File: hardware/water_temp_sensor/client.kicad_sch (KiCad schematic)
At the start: 7 parts, among them J1 AVR-ISP-6, U1 DS18B20, U2 DS18B20

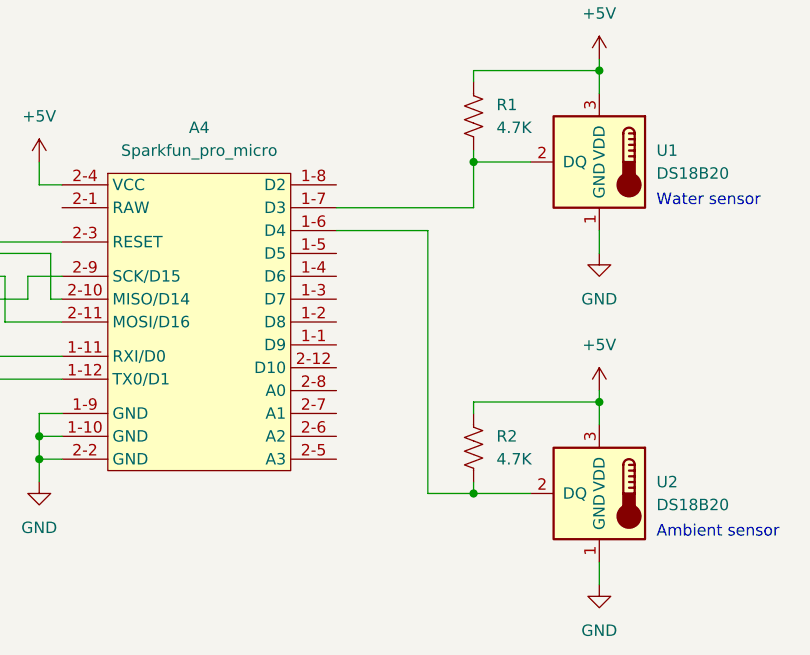
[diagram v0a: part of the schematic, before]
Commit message: Turn off status led for power reduction
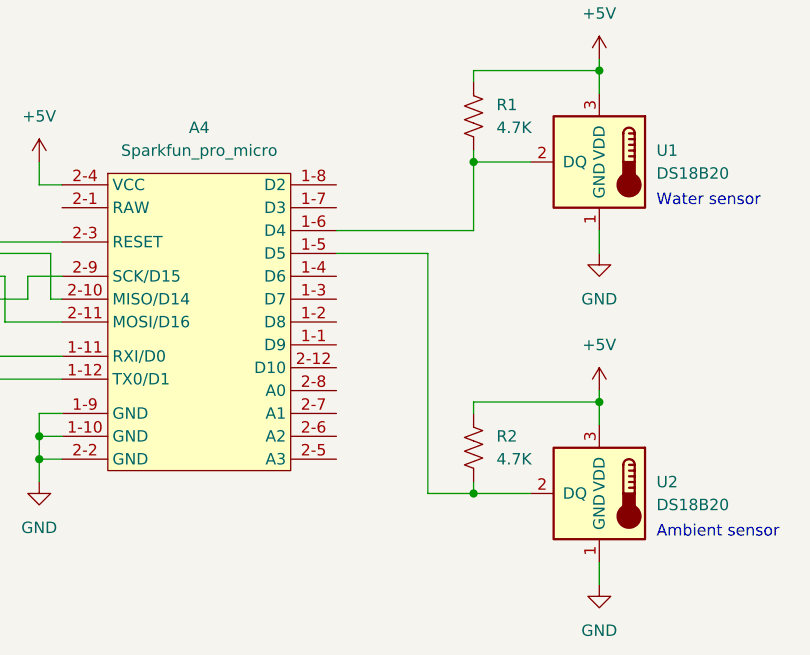
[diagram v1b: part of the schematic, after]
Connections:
- net at R1.2, U1.2 (DQ): now also A4.1-6 (D4); no longer A4.1-7 (D3)
- net at R2.2, U2.2 (DQ): now also A4.1-5 (D5); no longer A4.1-6 (D4)
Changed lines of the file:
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@@
-    (stroke (width 0) (type default) (color 0 0 0 0))
-  )
-  (wire (pts (xy 160.02 86.36) (xy 170.18 86.36))
     (stroke (width 0) (type default) (color 0 0 0 0))
   )
@@
     (stroke (width 0) (type default) (color 0 0 0 0))
   )
+  (wire (pts (xy 160.02 86.36) (xy 175.26 86.36))
+    (stroke (width 0) (type default) (color 0 0 0 0))
+  )
   (wire (pts (xy 93.98 104.14) (xy 93.98 106.68))
     (stroke (width 0) (type default) (color 0 0 0 0))
@@
   )
   (wire (pts (xy 127 81.28) (xy 129.54 81.28))
+    (stroke (width 0) (type default) (color 0 0 0 0))
+  )
+  (wire (pts (xy 175.26 78.74) (xy 175.26 86.36))
     (stroke (width 0) (type default) (color 0 0 0 0))
   )
@@
     (stroke (width 0) (type default) (color 0 0 0 0))
   )
-  (wire (pts (xy 160.02 83.82) (xy 175.26 83.82))
+  (wire (pts (xy 170.18 88.9) (xy 170.18 115.57))
     (stroke (width 0) (type default) (color 0 0 0 0))
   )
@@
     (stroke (width 0) (type default) (color 0 0 0 0))
   )
-  (wire (pts (xy 175.26 83.82) (xy 175.26 78.74))
-    (stroke (width 0) (type default) (color 0 0 0 0))
-  )
   (wire (pts (xy 189.23 105.41) (xy 189.23 107.95))
     (stroke (width 0) (type default) (color 0 0 0 0))
@@
     (stroke (width 0) (type default) (color 0 0 0 0))
   )
-  (wire (pts (xy 170.18 86.36) (xy 170.18 115.57))
-    (stroke (width 0) (type default) (color 0 0 0 0))
-  )
   (wire (pts (xy 175.26 77.47) (xy 175.26 78.74))
     (stroke (width 0) (type default) (color 0 0 0 0))
@@
     (stroke (width 0) (type default) (color 0 0 0 0))
   )
+  (wire (pts (xy 160.02 88.9) (xy 170.18 88.9))
+    (stroke (width 0) (type default) (color 0 0 0 0))
+  )

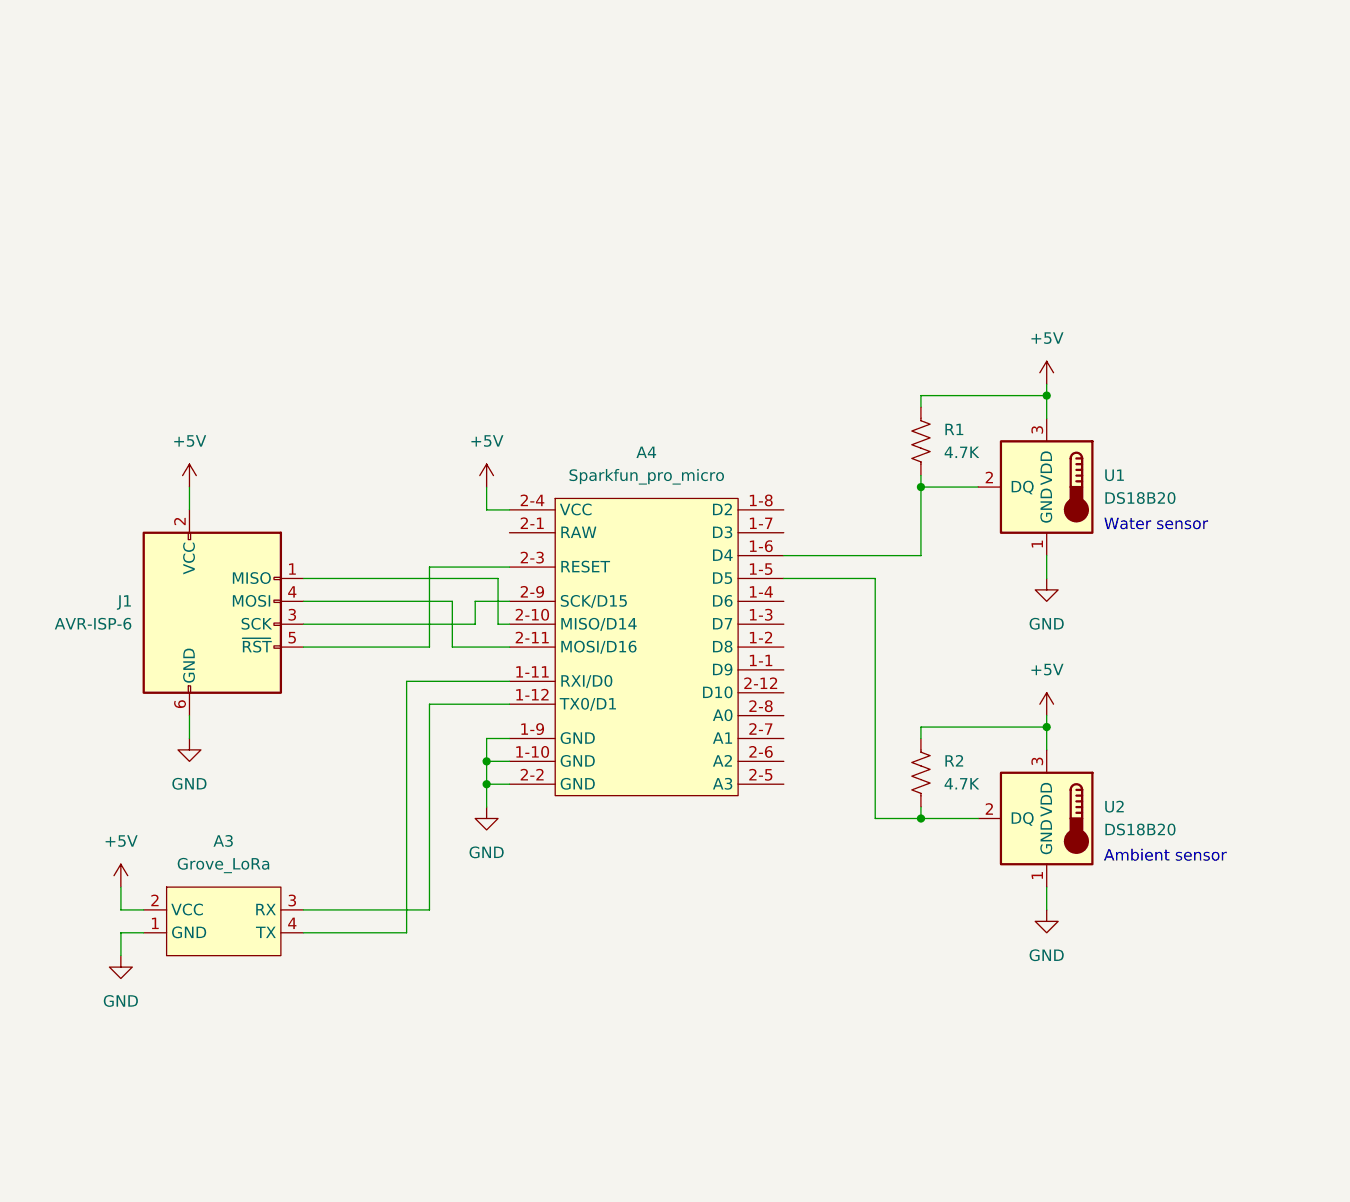
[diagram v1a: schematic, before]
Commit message: Turn off radio with mosfet to save power
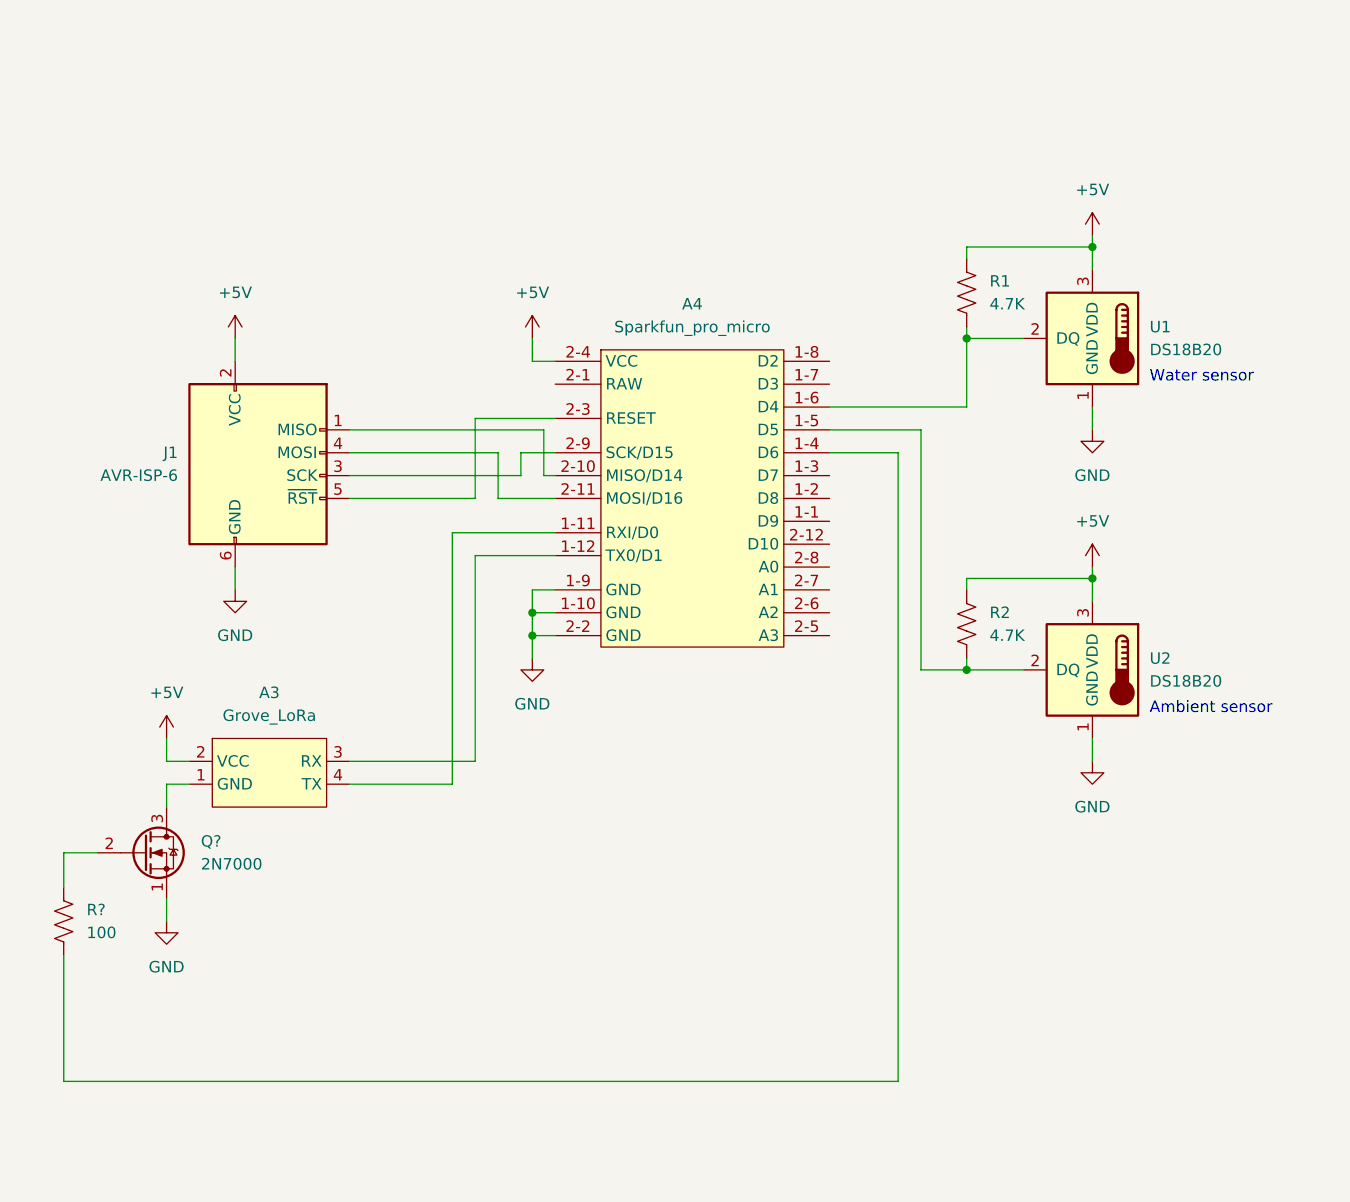
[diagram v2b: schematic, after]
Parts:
- added Q?: 2N7000, Package_TO_SOT_THT:TO-92_Inline, symbol Transistor_FET:2N7000
- added R?: 100, symbol Device:R_US
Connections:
- net GND: now also Q?.1 (S); no longer A3.1 (GND)
- net at A4.1-4 (D6): now also R?.2
- new net: A3.1 (GND), Q?.3 (D)
- new net: Q?.2 (G), R?.1
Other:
- moved on the sheet: A3, A4, J1, R1, R2, U1, U2

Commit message: Update schematic annotations
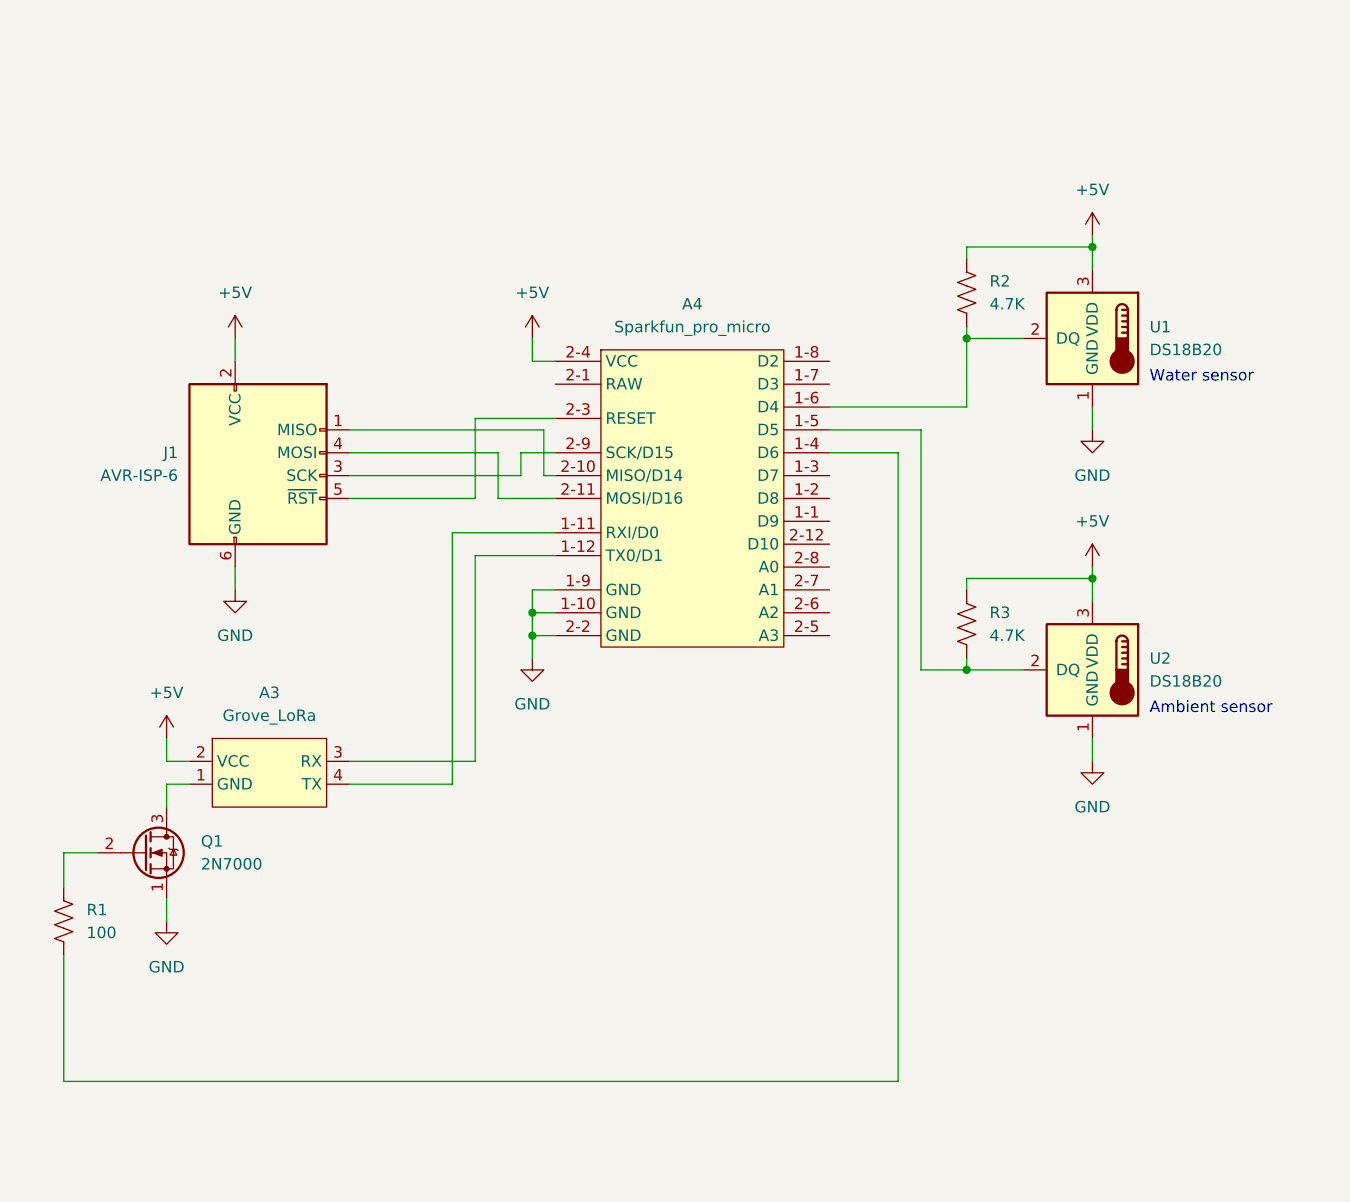
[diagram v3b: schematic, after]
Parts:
- gave numbers to parts that had none: 2
- renumbered R1 to R2, R2 to R3
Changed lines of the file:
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@@
   (symbol (lib_id "Device:R_US") (at 180.34 57.15 0) (unit 1)
     (in_bom yes) (on_board yes) (fields_autoplaced)
-    (property "Reference" "R1" (id 0) (at 182.88 55.8799 0)
+    (property "Reference" "R2" (id 0) (at 182.88 55.8799 0)
       (effects (font (size 1.27 1.27)) (justify left))
     )
@@
   (symbol (lib_id "Device:R_US") (at 180.34 93.98 0) (unit 1)
     (in_bom yes) (on_board yes) (fields_autoplaced)
-    (property "Reference" "R2" (id 0) (at 182.88 92.7099 0)
+    (property "Reference" "R3" (id 0) (at 182.88 92.7099 0)
       (effects (font (size 1.27 1.27)) (justify left))
     )
@@
   (symbol (lib_id "Device:R_US") (at 80.01 127 0) (unit 1)
     (in_bom yes) (on_board yes) (fields_autoplaced)
-    (property "Reference" "R?" (id 0) (at 82.55 125.7299 0)
+    (property "Reference" "R1" (id 0) (at 82.55 125.7299 0)
       (effects (font (size 1.27 1.27)) (justify left))
     )
@@
   (symbol (lib_id "Transistor_FET:2N7000") (at 88.9 119.38 0) (unit 1)
     (in_bom yes) (on_board yes) (fields_autoplaced)
-    (property "Reference" "Q?" (id 0) (at 95.25 118.1099 0)
+    (property "Reference" "Q1" (id 0) (at 95.25 118.1099 0)
       (effects (font (size 1.27 1.27)) (justify left))
     )

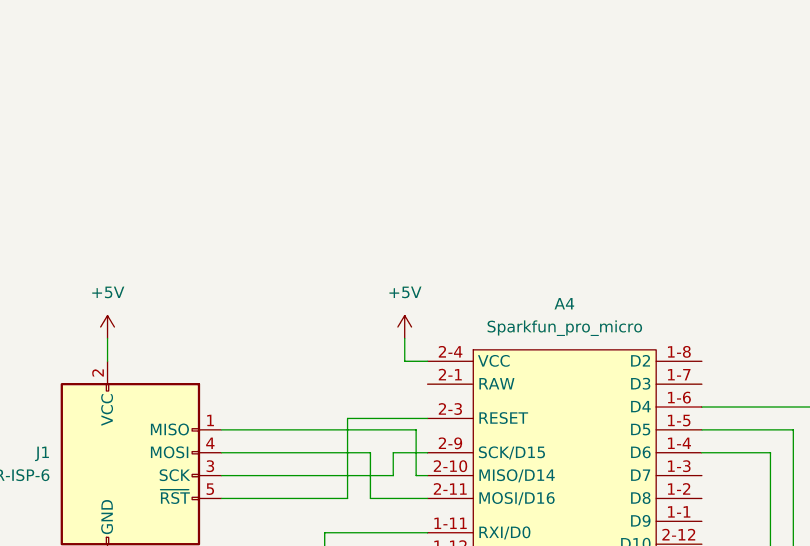
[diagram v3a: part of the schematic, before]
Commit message: Increase temperature sensor resolution
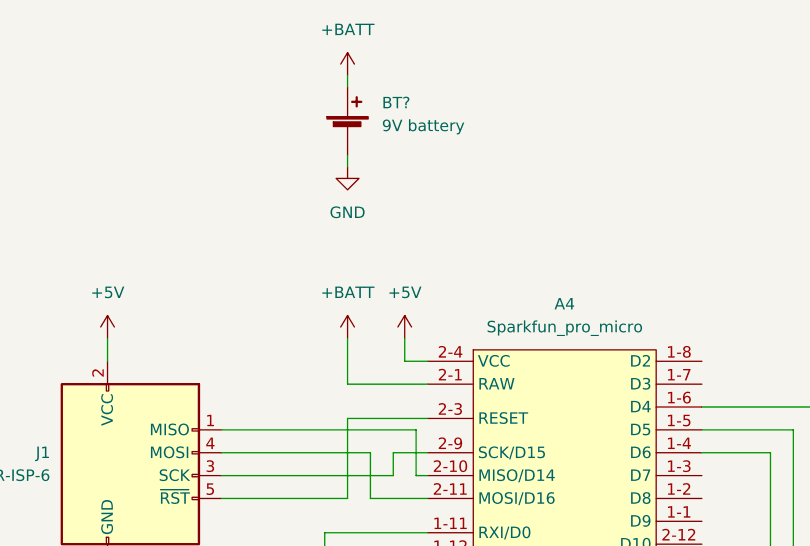
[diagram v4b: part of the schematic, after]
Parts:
- added BT?: 9V battery, symbol Device:Battery_Cell
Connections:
- net GND: now also BT?.2 (-)
- net +BATT: now reaches A4.2-1 (RAW)
- net +BATT: now also BT?.1 (+)
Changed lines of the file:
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@@
+    (stroke (width 0) (type default) (color 0 0 0 0))
+  )
+  (wire (pts (xy 125.73 33.02) (xy 125.73 34.29))
+    (stroke (width 0) (type default) (color 0 0 0 0))
+  )
+  (wire (pts (xy 125.73 41.91) (xy 125.73 43.18))
     (stroke (width 0) (type default) (color 0 0 0 0))
   )
@@
     (stroke (width 0) (type default) (color 0 0 0 0))
   )
+  (wire (pts (xy 125.73 67.31) (xy 134.62 67.31))
+    (stroke (width 0) (type default) (color 0 0 0 0))
+  )
   (wire (pts (xy 175.26 99.06) (xy 180.34 99.06))
     (stroke (width 0) (type default) (color 0 0 0 0))
@@
   )
   (wire (pts (xy 125.73 109.22) (xy 125.73 86.36))
+    (stroke (width 0) (type default) (color 0 0 0 0))
+  )
+  (wire (pts (xy 125.73 62.23) (xy 125.73 67.31))
     (stroke (width 0) (type default) (color 0 0 0 0))
   )
@@
     (pin "4")
   )
+  (symbol (lib_id "power:+BATT") (at 125.73 33.02 0) (unit 1)
+    (in_bom yes) (on_board yes) (fields_autoplaced)
+    (property "Reference" "#PWR?" (id 0) (at 125.73 36.83 0)
+      (effects (font (size 1.27 1.27)) hide)
+    )
+    (property "Value" "+BATT" (id 1) (at 125.73 27.94 0))
+    (property "Footprint" "" (id 2) (at 125.73 33.02 0)
+      (effects (font (size 1.27 1.27)) hide)
+    )
+    (property "Datasheet" "" (id 3) (at 125.73 33.02 0)
+      (effects (font (size 1.27 1.27)) hide)
+    )
+    (pin "1")
+  )
   (symbol (lib_id "power:+5V") (at 99.06 62.23 0) (unit 1)
     (in_bom yes) (on_board yes) (fields_autoplaced)
@@
     )
     (property "Datasheet" "" (id 3) (at 99.06 62.23 0)
+      (effects (font (size 1.27 1.27)) hide)
+    )
+    (pin "1")
+  )
+  (symbol (lib_id "power:GND") (at 125.73 43.18 0) (unit 1)
+    (in_bom yes) (on_board yes) (fields_autoplaced)
+    (property "Reference" "#PWR?" (id 0) (at 125.73 49.53 0)
+      (effects (font (size 1.27 1.27)) hide)
+    )
+    (property "Value" "GND" (id 1) (at 125.73 48.26 0))
+    (property "Footprint" "" (id 2) (at 125.73 43.18 0)
+      (effects (font (size 1.27 1.27)) hide)
+    )
+    (property "Datasheet" "" (id 3) (at 125.73 43.18 0)
       (effects (font (size 1.27 1.27)) hide)
     )
@@
     (pin "2-9")
   )
+  (symbol (lib_id "Device:Battery_Cell") (at 125.73 39.37 0) (unit 1)
+    (in_bom yes) (on_board yes) (fields_autoplaced)
+    (property "Reference" "BT?" (id 0) (at 129.54 36.0679 0)
+      (effects (font (size 1.27 1.27)) (justify left))
+    )
+    (property "Value" "9V battery" (id 1) (at 129.54 38.6079 0)
+      (effects (font (size 1.27 1.27)) (justify left))
+    )
+    (property "Footprint" "" (id 2) (at 125.73 37.846 90)
+      (effects (font (size 1.27 1.27)) hide)
+    )
+    (property "Datasheet" "~" (id 3) (at 125.73 37.846 90)
+      (effects (font (size 1.27 1.27)) hide)
+    )
+    (pin "1")
+    (pin "2")
+  )
   (symbol (lib_id "Sensor_Temperature:DS18B20") (at 194.31 99.06 0) (mirror y) (unit 1)
     (in_bom yes) (on_board yes) (fields_autoplaced)
@@
     (pin "3")
   )
+  (symbol (lib_id "power:+BATT") (at 125.73 62.23 0) (unit 1)
+    (in_bom yes) (on_board yes) (fields_autoplaced)
+    (property "Reference" "#PWR?" (id 0) (at 125.73 66.04 0)
+      (effects (font (size 1.27 1.27)) hide)
+    )
+    (property "Value" "+BATT" (id 1) (at 125.73 57.15 0))
+    (property "Footprint" "" (id 2) (at 125.73 62.23 0)
+      (effects (font (size 1.27 1.27)) hide)
+    )
+    (property "Datasheet" "" (id 3) (at 125.73 62.23 0)
+      (effects (font (size 1.27 1.27)) hide)
+    )
+    (pin "1")
+  )
 )

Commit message: Update schematic
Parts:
- gave numbers to parts that had none: 1
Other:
- moved on the sheet: A3, A4, BT1, J1, Q1, R1, R2, R3, U1, U2
